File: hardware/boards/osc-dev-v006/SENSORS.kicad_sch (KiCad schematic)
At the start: 46 parts, among them J5 POS, J6 ENC, J7 NTC

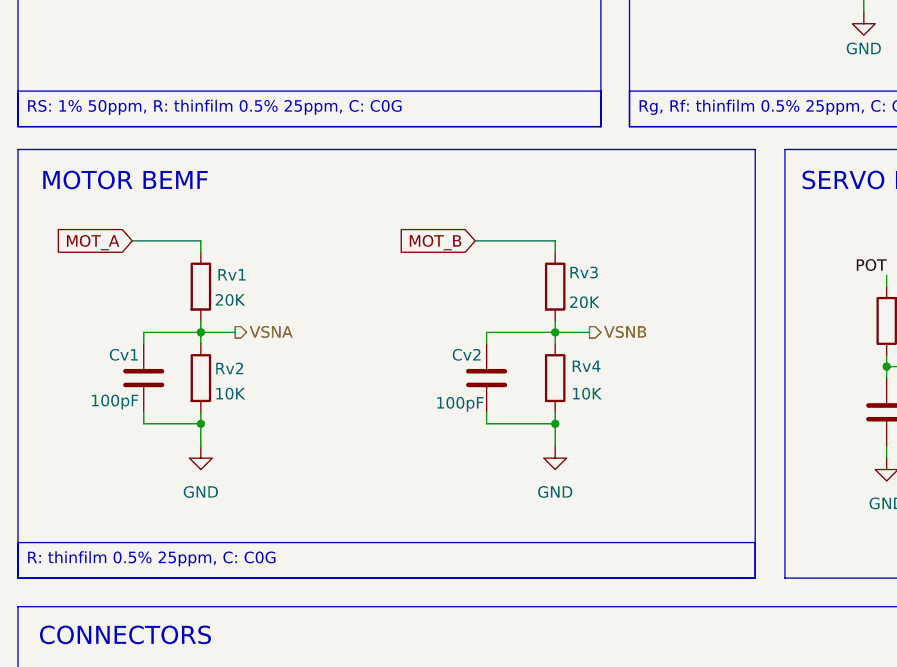
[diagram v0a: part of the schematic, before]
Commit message: board: v006 rev-2a refresh in progress, vsns divider placed, tel uart removed
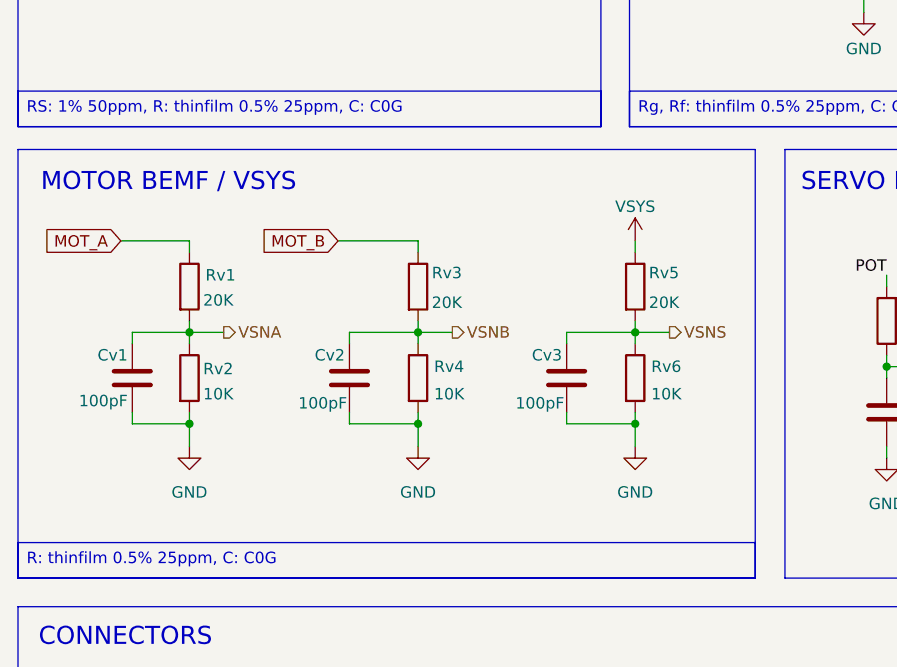
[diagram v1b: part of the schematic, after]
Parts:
- added Cv3: 100pF, Capacitor_SMD:C_0603_1608Metric_Pad1.08x0.95mm_HandSolder, symbol Device:C
- added Rv5: 20K, Resistor_SMD:R_0603_1608Metric_Pad0.98x0.95mm_HandSolder, symbol Device:R
- added Rv6: 10K, Resistor_SMD:R_0603_1608Metric_Pad0.98x0.95mm_HandSolder, symbol Device:R
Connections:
- net GND: now also Cv3.2, Rv6.2
- new net VSNS: Cv3.1, Rv5.2, Rv6.1
- new net VSYS: Rv5.1
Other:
- note added: "MOTOR BEMF / VSYS"
- note removed: "MOTOR BEMF"
- moved on the sheet: Cv1, Cv2, Rv1, Rv2, Rv3, Rv4

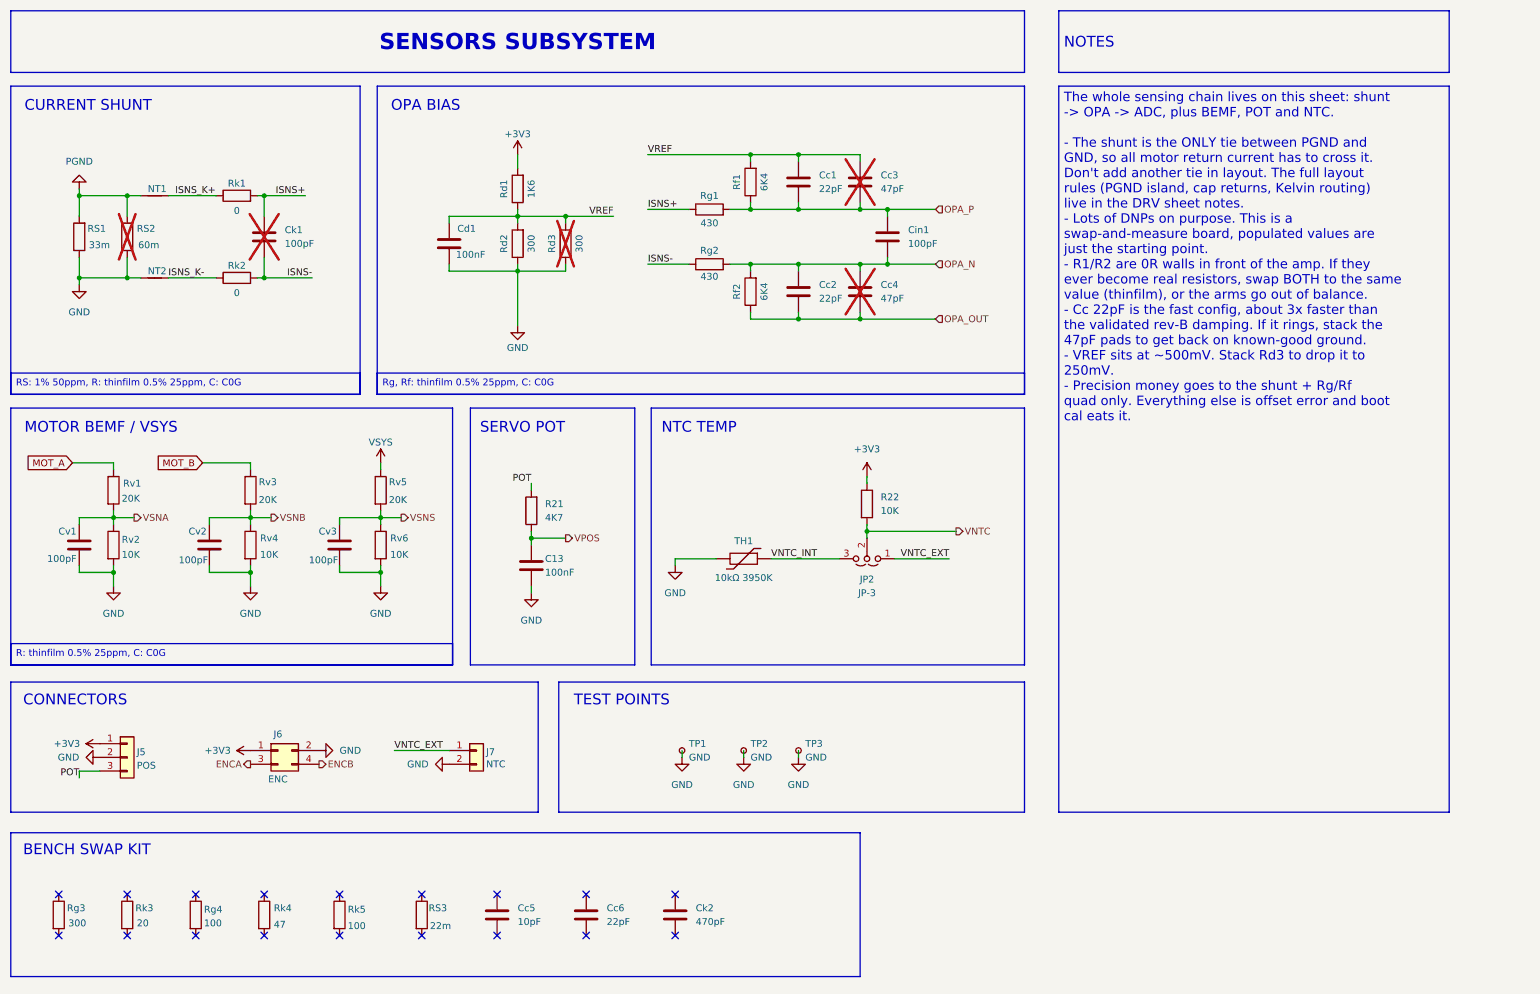
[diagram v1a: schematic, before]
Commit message: board: v006 rev-2a schematic refresh, family designators, terminal bias, tier-2 position input
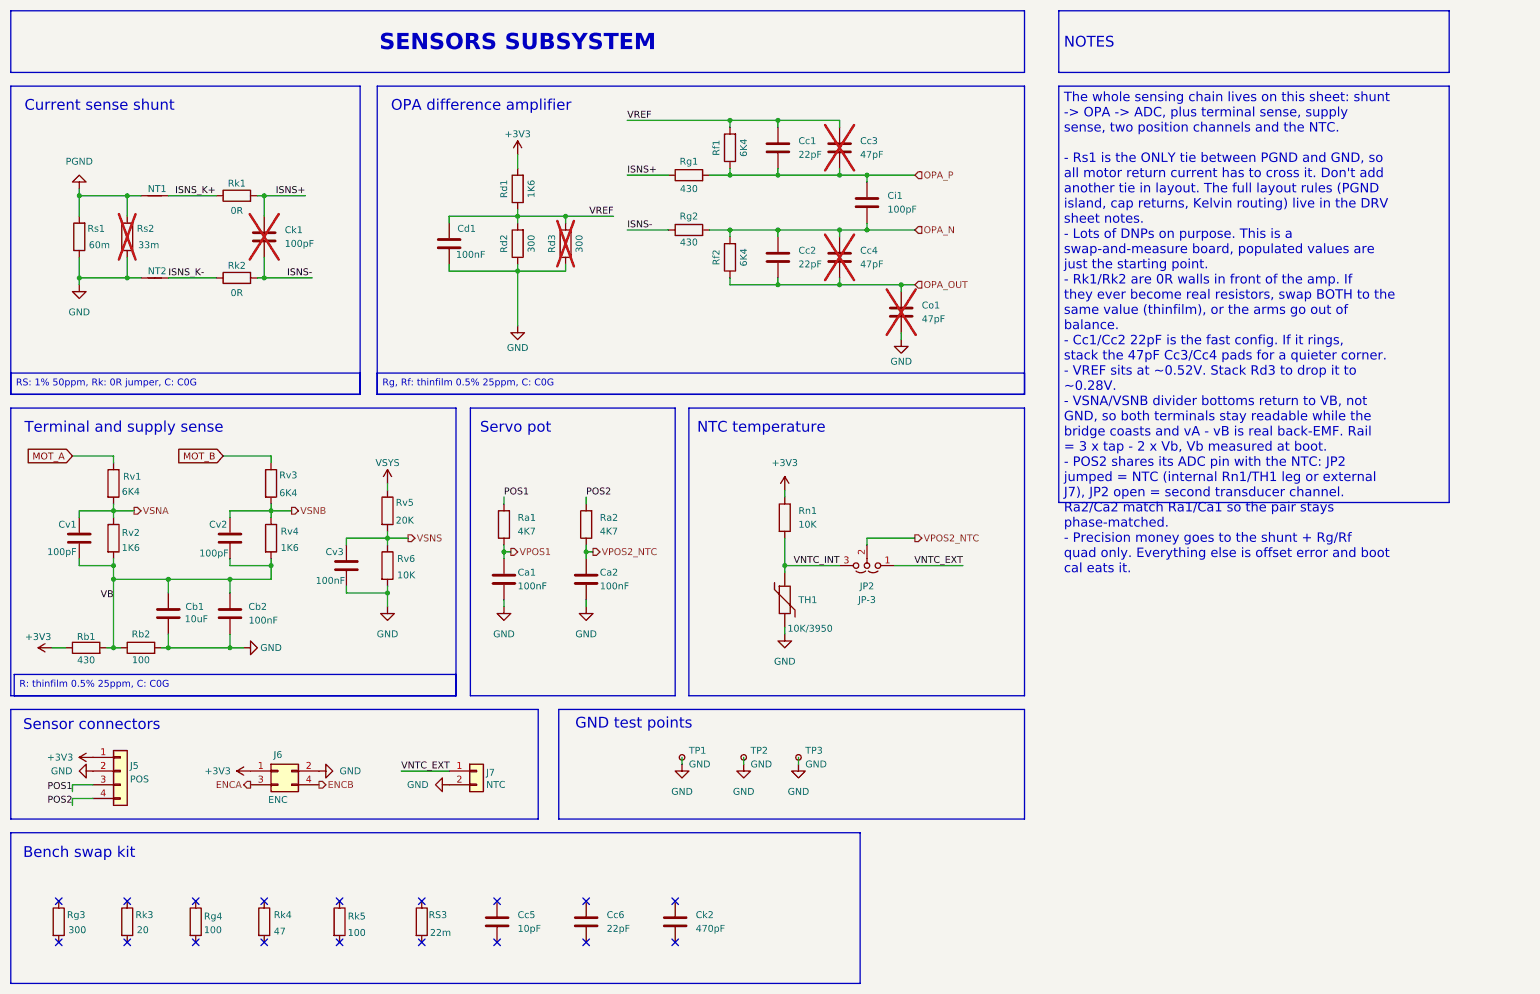
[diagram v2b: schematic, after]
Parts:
- removed R22: 10K, Resistor_SMD:R_0603_1608Metric_Pad0.98x0.95mm_HandSolder, symbol Device:R
- added Ca2, Cb2: 100nF, Capacitor_SMD:C_0603_1608Metric_Pad1.08x0.95mm_HandSolder, symbol Device:C
- added Cb1: 10uF, Capacitor_SMD:C_0805_2012Metric_Pad1.18x1.45mm_HandSolder, symbol Device:C
- added Co1: 47pF, Capacitor_SMD:C_0603_1608Metric_Pad1.08x0.95mm_HandSolder, symbol Device:C
- added Ra2: 4K7, Resistor_SMD:R_0603_1608Metric_Pad0.98x0.95mm_HandSolder, symbol Device:R
- added Rb1: 430, Resistor_SMD:R_0603_1608Metric_Pad0.98x0.95mm_HandSolder, symbol Device:R
- added Rb2: 100, Resistor_SMD:R_0603_1608Metric_Pad0.98x0.95mm_HandSolder, symbol Device:R
- added Rn1: 10K, Resistor_SMD:R_0603_1608Metric_Pad0.98x0.95mm_HandSolder, symbol Device:R
- Ck1: JLC_Basic yes -> (none)
- Cv3: value 100pF -> 100nF; LCSC C14665 -> C14663; MFPN CC0603JRNPO9BN101 -> CC0603KRX7R9BB104
- J5: footprint Connector_PinHeader_2.54mm:PinHeader_1x03_P2.54mm_Vertical -> Connector_PinHeader_2.54mm:PinHeader_1x04_P2.54mm_Vertical; symbol Connector_Generic:Conn_01x03 -> Connector_Generic:Conn_01x04; LCSC C49257 -> (none); MFPN 2.54-1*3P -> 2.54-1*4P
- Ra1: renamed from R21; MFPN FRC0805F4701TS -> FRC0603F4701TS
- Rd1: MFPN FRC0805F1001TS -> AR03DTC1601
- Rd2: MFPN FRC0805F1800TS -> AR03DTC3000
- Rd3: MFPN FRC0805F1500TS -> AR03DTC3000
- Rf1, Rf2: MFPN ARG03DTC7501 -> AR03DTC6401N
- Rg1, Rg2: MFPN ARG03DTC4990 -> AR03DTCX4300
- Rg3: MFPN ARG03DTC2500 -> AR03DTC3000
- Rg4: MFPN ARG03DTC1200 -> AR03DTCX1000
- Rk1, Rk2: value 0 -> 0R
- Rk5: MFPN FRC0805F47R0TS -> AR03DTCX1000
- Rs1: renamed from RS1; value 33m -> 60m; LCSC C49164942 -> C49164944; MFPN JER1206F1R033 -> JER1206F1R060
- Rs2: renamed from RS2; value 60m -> 33m; LCSC C49164944 -> C49164942; MFPN JER1206F1R060 -> JER1206F1R033
- Rv1, Rv3: value 20K -> 6K4; LCSC C319764 -> C374580; MFPN ARG03DTC2002 -> AR03DTC6401N
- Rv2, Rv4: value 10K -> 1K6; LCSC C319937 -> C374557; MFPN ARG02DTC1002 -> AR03DTC1601
- Rv5: MFPN ARG03DTC2002 -> AR03DTCX2002
- Rv6: MFPN ARG02DTC1002 -> AR03DTCX1002
- TH1: value 10kΩ 3950K -> 10K/3950; MFPN SDNT2012X103F3950FTF -> CMFA103F3950
- TP1, TP2, TP3: now left out of the parts list
- renumbered C13 to Ca1, Cin1 to Ci1
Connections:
- net +3V3: now also Rb1.1, Rn1.1
- net GND: now also Ca2.2, Cb1.2, Cb2.2, Co1.2, Rb2.2; no longer Cv1.2, Cv2.2, Rv2.2, Rv4.2
- net OPA_OUT: now also Co1.1
- net VNTC_INT: now also Rn1.2
- net POT renamed POS1
- net VNTC renamed VPOS2_NTC
- net VPOS2_NTC: now also Ca2.1, Ra2.1
- net VPOS renamed VPOS1
- new net POS2: J5.4 (Pin_4), Ra2.2
- new net VB: Cb1.1, Cb2.1, Cv1.2, Cv2.2, Rb1.2, Rb2.1, Rv2.2, Rv4.2
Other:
- note added: "Bench swap kit"
- note added: "Current sense shunt"
- note added: "GND test points"
- note added: "NTC temperature"
- note added: "OPA difference amplifier"
- note added: "Sensor connectors"
- note added: "Servo pot"
- note added: "Terminal and supply sense"
- note removed: "BENCH SWAP KIT"
- note removed: "CONNECTORS"
- note removed: "CURRENT SHUNT"
- note removed: "MOTOR BEMF / VSYS"
- note removed: "NTC TEMP"
- note removed: "OPA BIAS"
- note removed: "SERVO POT"
- note removed: "TEST POINTS"
- moved on the sheet: Ca1, Cc1, Cc2, Cc3, Cc4, Cc5, Cc6, Ci1, Ck2, Cv3, J6, J7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

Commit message: board: v006 rev-2a audit fixes, rs2 deleted, rh2 jumper on the driver rail
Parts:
- removed Cc5: 10pF, Capacitor_SMD:C_0603_1608Metric_Pad1.08x0.95mm_HandSolder, symbol Device:C
- removed Cc6: 22pF, Capacitor_SMD:C_0603_1608Metric_Pad1.08x0.95mm_HandSolder, symbol Device:C
- removed Ck2: 470pF, Capacitor_SMD:C_0603_1608Metric_Pad1.08x0.95mm_HandSolder, symbol Device:C
- removed RS3: 22m, Resistor_SMD:R_1206_3216Metric, symbol Device:R
- removed Rg3: 300, Resistor_SMD:R_0603_1608Metric_Pad0.98x0.95mm_HandSolder, symbol Device:R
- removed Rg4, Rk5: 100, Resistor_SMD:R_0603_1608Metric_Pad0.98x0.95mm_HandSolder, symbol Device:R
- removed Rk3: 20, Resistor_SMD:R_0603_1608Metric_Pad0.98x0.95mm_HandSolder, symbol Device:R
- removed Rk4: 47, Resistor_SMD:R_0603_1608Metric_Pad0.98x0.95mm_HandSolder, symbol Device:R
- removed Rs2: 33m, Resistor_SMD:R_1206_3216Metric, symbol Device:R
- Cc3, Cc4: value 47pF -> 22pF; LCSC C1671 -> C105620; MFPN CC0805JRNPO9BN470 -> CC0603JRNPO9BN220
- Co1: value 47pF -> 100pF; LCSC C1671 -> C14665; MFPN CC0805JRNPO9BN470 -> CC0603JRNPO9BN101
- Cv3: value 100nF -> 100pF; LCSC C14663 -> C14665; MFPN CC0603KRX7R9BB104 -> CC0603JRNPO9BN101
- J7: footprint Connector_PinHeader_2.54mm:PinHeader_1x02_P2.54mm_Vertical -> Connector_PinHeader_2.54mm:PinHeader_1x03_P2.54mm_Vertical; symbol Connector_Generic:Conn_01x02 -> Connector_Generic:Conn_01x03; LCSC C492401 -> C49257; MFPN 2.54-1*2P -> 2.54-1*3P
- Rv5: value 20K -> 6K4; LCSC C319764 -> C374580; MFPN AR03DTCX2002 -> AR03DTC6401N
- Rv6: value 10K -> 1K6; LCSC C319937 -> C374557; MFPN AR03DTCX1002 -> AR03DTC1601
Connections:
- net +3V3: now also J7.2 (Pin_2)
- net GND: now also J7.3 (Pin_3); no longer J7.2 (Pin_2)
- no-connect marks 18 -> 0
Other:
- note removed: "Bench swap kit"
- moved on the sheet: Ck1, NT1, NT2, Rk1, Rk2, Rs1

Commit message: board: v006 rev-2a flex landing j11, rs1 hand-solder footprint
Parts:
- added J11: Conn_01x06, shared:Flex_Landing_1x06_P1.0mm, symbol Connector_Generic:Conn_01x06
- Rs1: footprint Resistor_SMD:R_1206_3216Metric -> Resistor_SMD:R_1206_3216Metric_Pad1.30x1.75mm_HandSolder
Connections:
- net +3V3: now also J11.2 (Pin_2)
- net ENCA: now also J11.3 (Pin_3)
- net ENCB: now also J11.4 (Pin_4)
- net GND: now also J11.1 (Pin_1), J11.6 (Pin_6)
- net VNTC_EXT: now also J11.5 (Pin_5)

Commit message: board: v006 rev-2a placement, silk labels, test point rows, silk rules
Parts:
- removed TP3: GND, TestPoint:TestPoint_Pad_D1.0mm, symbol Connector:TestPoint_Small
- added TP5: VA, TestPoint:TestPoint_Pad_D1.0mm, symbol Connector:TestPoint_Small
- added TP6: VB, TestPoint:TestPoint_Pad_D1.0mm, symbol Connector:TestPoint_Small
- added TP7: VS, TestPoint:TestPoint_Pad_D1.0mm, symbol Connector:TestPoint_Small
- added TP8: VP1, TestPoint:TestPoint_Pad_D1.0mm, symbol Connector:TestPoint_Small
- added TP9: VP2, TestPoint:TestPoint_Pad_D1.0mm, symbol Connector:TestPoint_Small
- TP2: value GND -> OPA
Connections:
- net GND: no longer TP2.1
- net OPA_OUT: now also TP2.1
- net VPOS1: now also TP8.1
- net VPOS2_NTC: now also TP9.1
- net VSNA: now also TP5.1
- net VSNB: now also TP6.1
- net VSNS: now also TP7.1
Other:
- note removed: "GND test points"
